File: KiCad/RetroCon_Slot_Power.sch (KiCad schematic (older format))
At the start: 35 parts, among them J1 POWER, J17 USB_A_DUAL, J7 POWER-OUT, SW1 SW_SPDT, SW2 SW_SPDT, SW3 SW_DPDT, U5 PUD-0512, U6 MDD02L-12, U8 LM1117-33

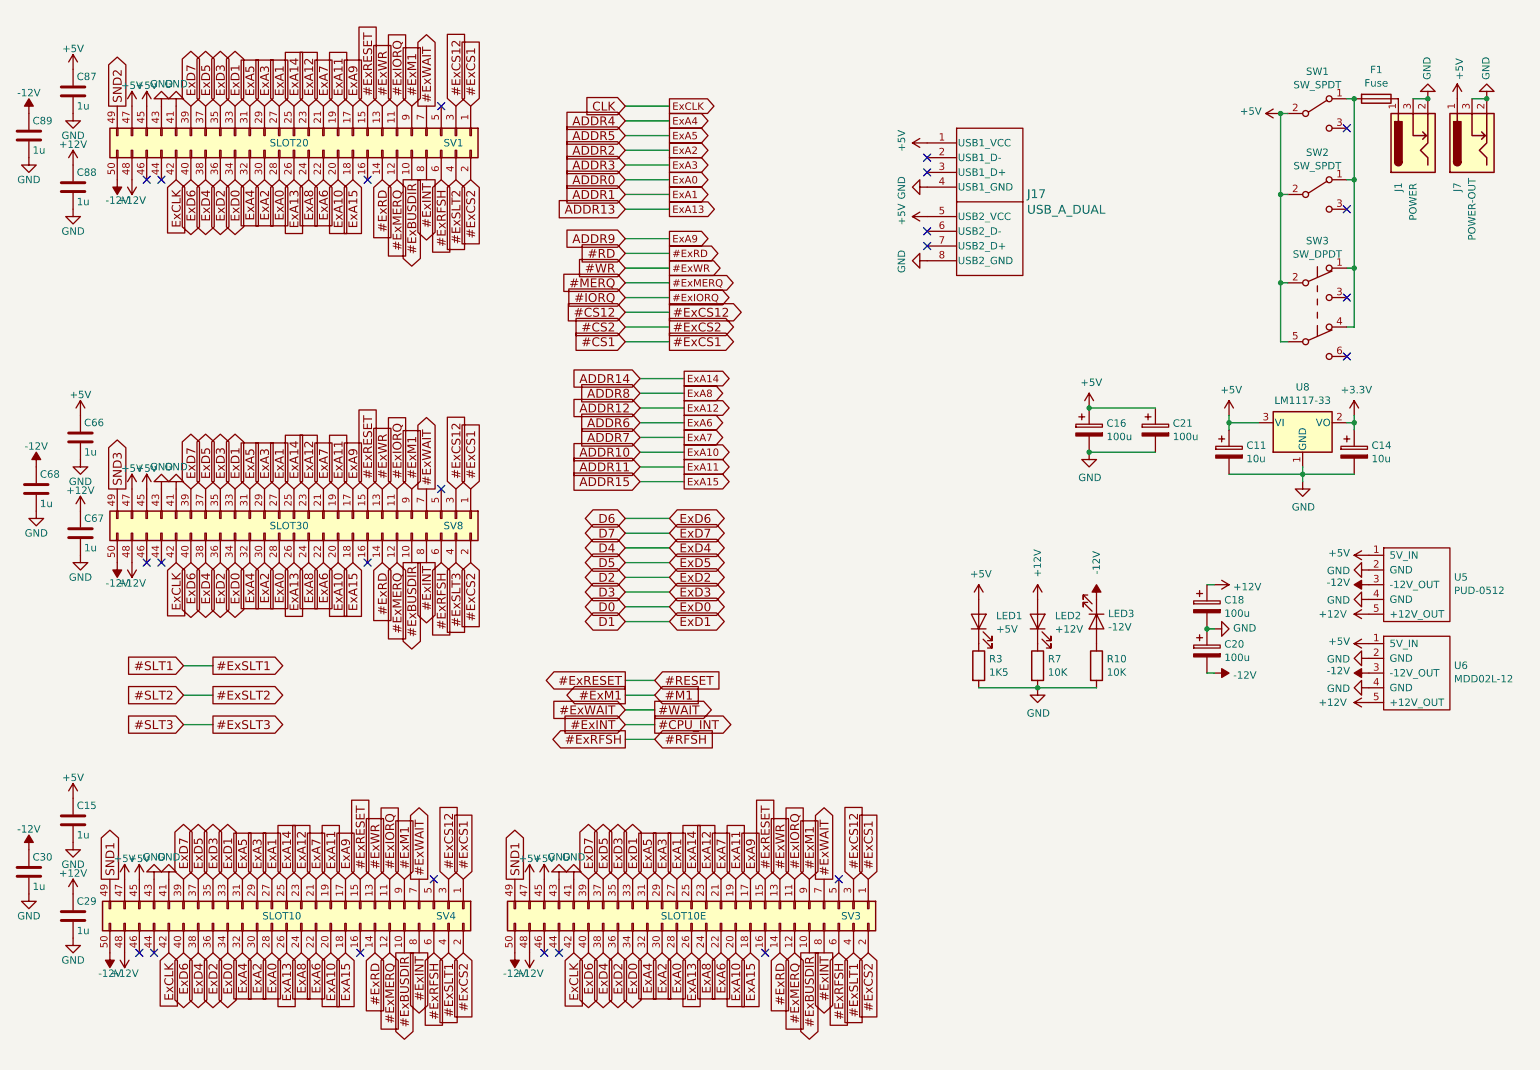
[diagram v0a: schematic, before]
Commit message: fix up some details
change proper value of Capacitor for XTAL
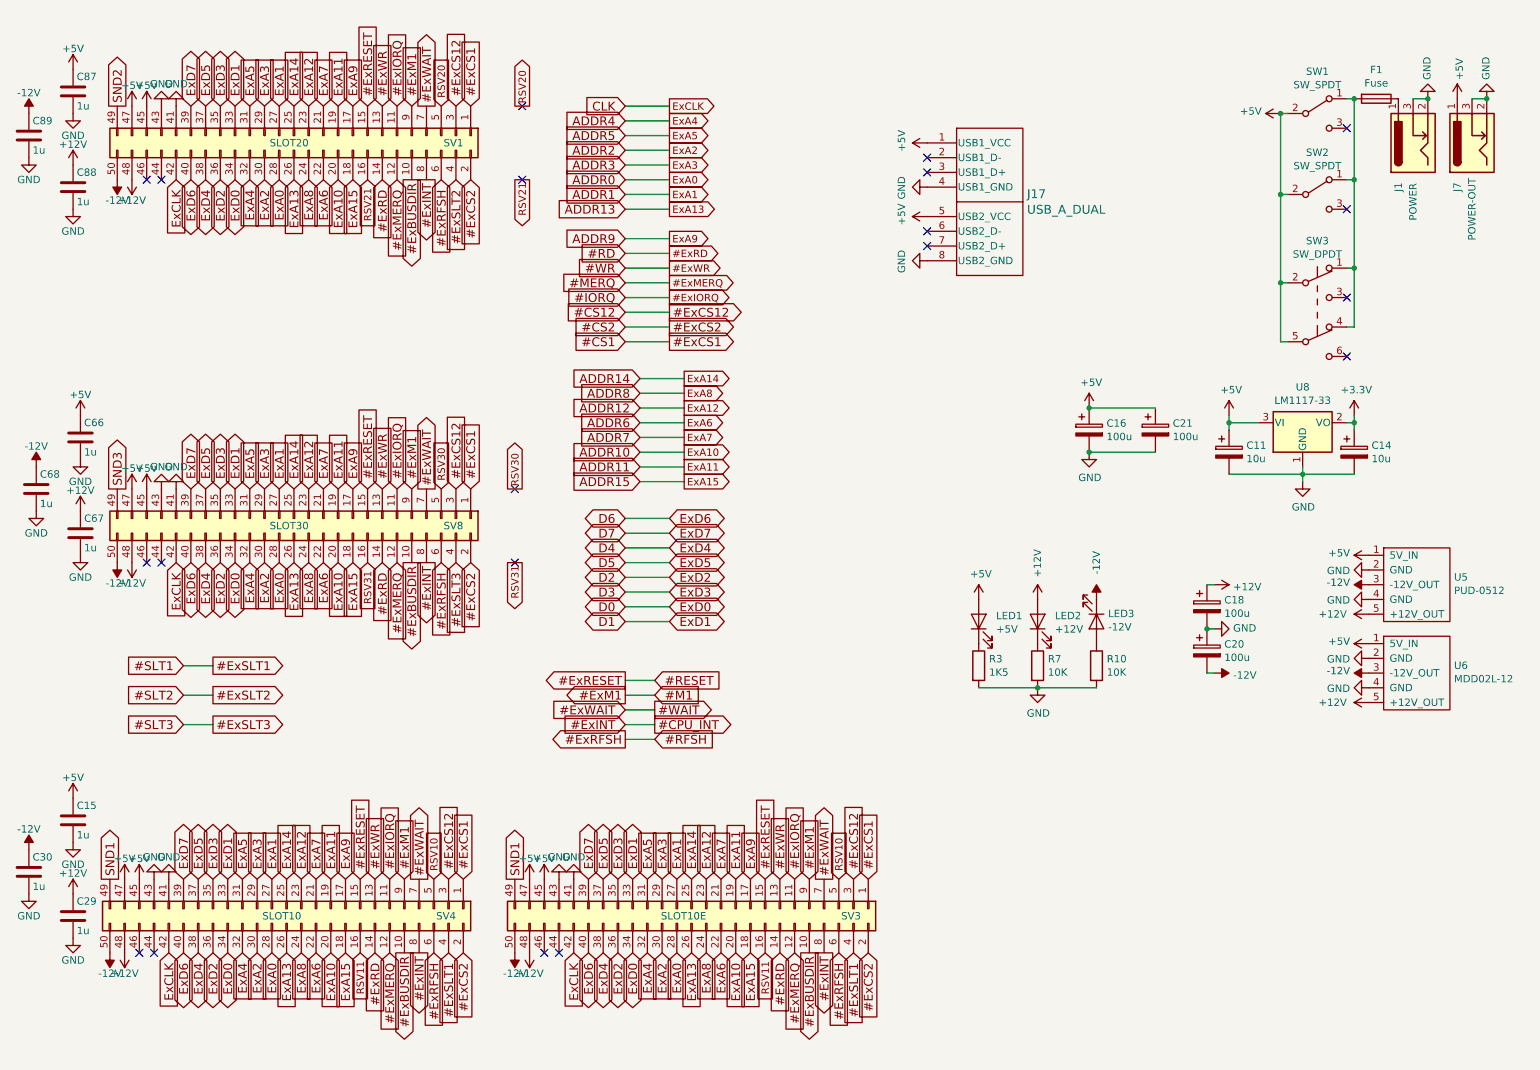
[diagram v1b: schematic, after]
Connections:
- net RSV31: now reaches SV8.16 (Pin_16)
- net RSV30: now reaches SV8.5 (Pin_5)
- net RSV21: now reaches SV1.16 (Pin_16)
- net RSV20: now reaches SV1.5 (Pin_5)
- net RSV11: now reaches SV4.16 (Pin_16)
- net RSV11: now also SV3.16 (Pin_16)
- net RSV10: now reaches SV4.5 (Pin_5)
- net RSV10: now also SV3.5 (Pin_5)
- no-connect marks 24 -> 20
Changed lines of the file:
@@
 	1    0    0    -1
 $EndComp
-NoConn ~ 3550 6350
-NoConn ~ 3050 6850
 $Comp
 L power:GND #PWR?
@@
 Text GLabel 6400 6850 3    60   Input ~ 0
 #ExSLT1
-NoConn ~ 6300 6350
-NoConn ~ 5800 6850
 Text GLabel 6500 6350 1    60   Input ~ 0
 #ExCS1
@@
 Text GLabel 6100 6850 3    60   Output ~ 0
 #ExBUSDIR
-NoConn ~ 3100 4200
-NoConn ~ 3600 3700
-NoConn ~ 3100 1600
-NoConn ~ 3600 1100
 $Comp
 L RetroConT-rescue:PUD-0512-cloudree_dcdc U5
@@
 	9300 2700 9350 2700
 Connection ~ 9300 2300
+Text GLabel 3600 1100 1    50   Input ~ 0
+RSV20
+Text GLabel 3100 1600 3    50   Input ~ 0
+RSV21
+Text GLabel 4150 1100 1    50   Output ~ 0
+RSV20
+Text GLabel 4150 1600 3    50   Output ~ 0
+RSV21
+NoConn ~ 4150 1100
+NoConn ~ 4150 1600
+Text GLabel 3600 3700 1    50   Input ~ 0
+RSV30
+Text GLabel 3100 4200 3    50   Input ~ 0
+RSV31
+Text GLabel 4100 3700 1    50   Output ~ 0
+RSV30
+Text GLabel 4100 4200 3    50   Output ~ 0
+RSV31
+NoConn ~ 4100 3700
+NoConn ~ 4100 4200
+Text GLabel 3550 6350 1    50   Input ~ 0
+RSV10
+Text GLabel 3050 6850 3    50   Input ~ 0
+RSV11
+Text GLabel 5800 6850 3    50   Input ~ 0
+RSV11
+Text GLabel 6300 6350 1    50   Input ~ 0
+RSV10
 $EndSCHEMATC
